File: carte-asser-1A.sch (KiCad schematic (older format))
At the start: 0 parts

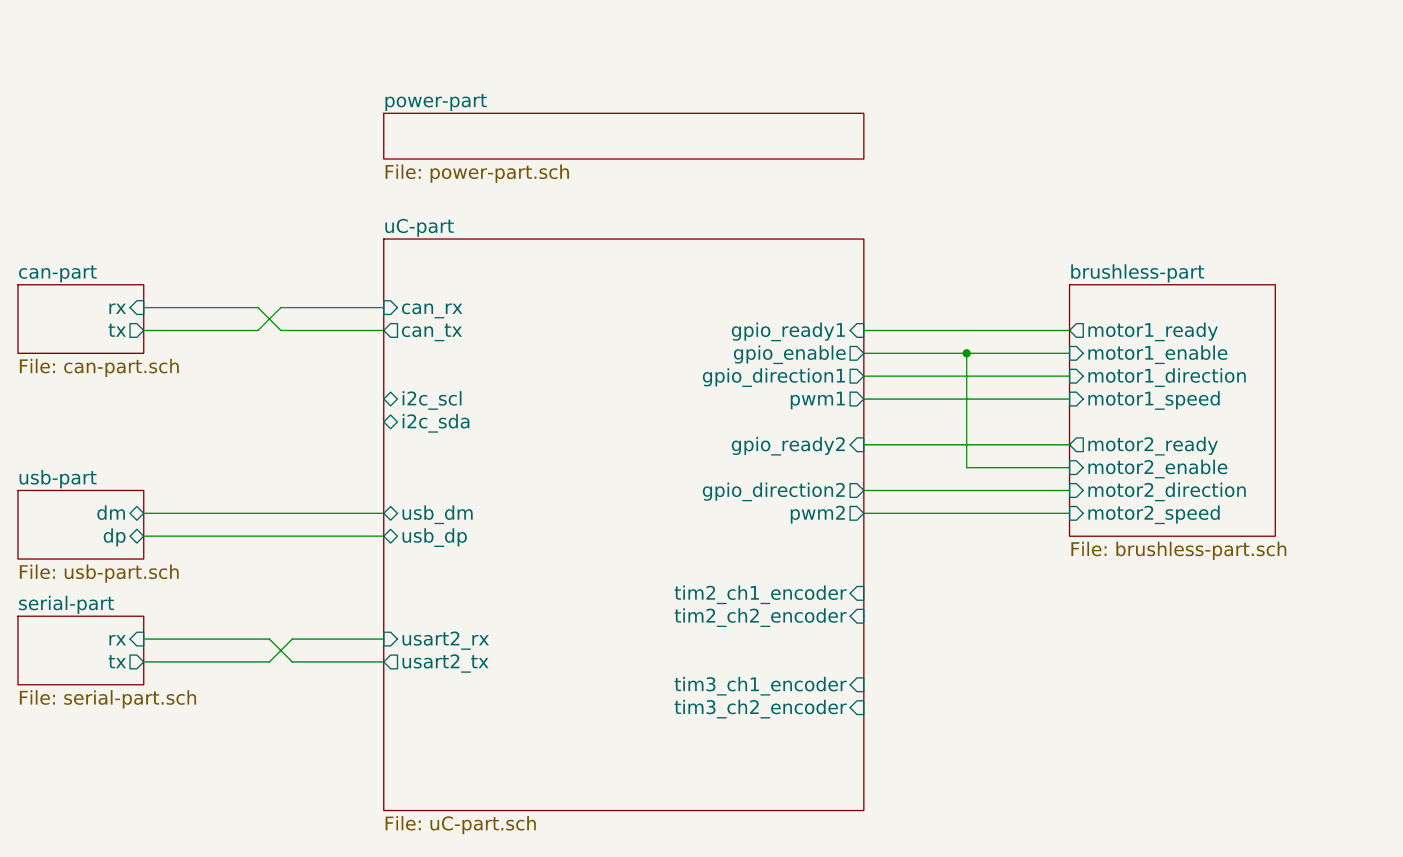
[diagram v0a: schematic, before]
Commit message: schematic seems ok, ongoing routing
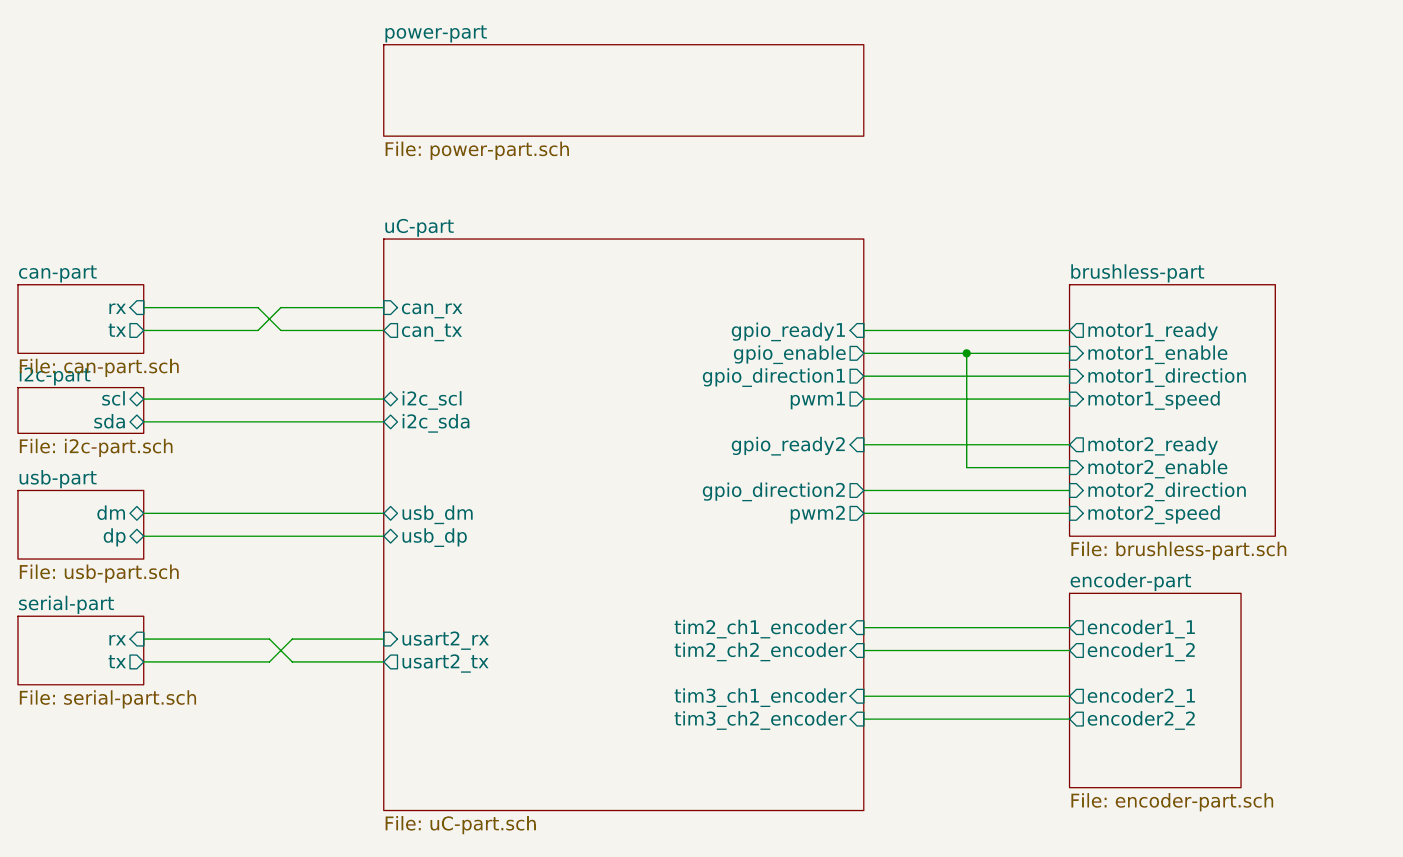
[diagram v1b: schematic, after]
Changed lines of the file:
@@
 $Descr A4 11693 8268
 encoding utf-8
-Sheet 1 7
+Sheet 1 9
 Title ""
 Date ""
@@
 F4 "i2c_sda" B L 5000 2950 60
 F5 "i2c_scl" B L 5000 2850 60
-F6 "tim2_ch2_encoder" I R 7100 3800 60
-F7 "tim2_ch1_encoder" I R 7100 3700 60
-F8 "tim3_ch2_encoder" I R 7100 4200 60
-F9 "tim3_ch1_encoder" I R 7100 4100 60
+F6 "tim2_ch2_encoder" I R 7100 3950 60
+F7 "tim2_ch1_encoder" I R 7100 3850 60
+F8 "tim3_ch2_encoder" I R 7100 4250 60
+F9 "tim3_ch1_encoder" I R 7100 4150 60
 F10 "usart2_rx" I L 5000 3900 60
 F11 "usart2_tx" O L 5000 4000 60
@@
 $EndSheet
 $Sheet
-S 5000 1600 2100 200
+S 5000 1300 2100 400
 U 57013891
 F0 "power-part" 60
@@
 Wire Wire Line
 	4600 3900 5000 3900
+$Sheet
+S 8000 3700 750  850
+U 5707AF1F
+F0 "encoder-part" 60
+F1 "encoder-part.sch" 60
+F2 "encoder1_1" O L 8000 3850 60
+F3 "encoder1_2" O L 8000 3950 60
+F4 "encoder2_1" O L 8000 4150 60
+F5 "encoder2_2" O L 8000 4250 60
+$EndSheet
+Wire Wire Line
+	7100 3850 8000 3850
+Wire Wire Line
+	7100 3950 8000 3950
+Wire Wire Line
+	7100 4150 8000 4150
+Wire Wire Line
+	7100 4250 8000 4250
+Wire Wire Line
+	5000 2950 3950 2950
+Wire Wire Line
+	3950 2850 5000 2850
+$Sheet
+S 3400 2800 550  200
+U 570700AB
+F0 "i2c-part" 60
+F1 "i2c-part.sch" 60
+F2 "sda" B R 3950 2950 60
+F3 "scl" B R 3950 2850 60
+$EndSheet
 $EndSCHEMATC
